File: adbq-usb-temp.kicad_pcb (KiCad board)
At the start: 4 copper layers, 75 parts, among them J4 USB_C_Receptacle_USB2.0_14P, Q1 Q_NMOS, Q2 Q_NMOS, Q3 Q_NMOS, SW1 SW_Push, SW2 TestPoint, SW3 TestPoint, SW4 TestPoint, U1 ESP32-S3FH4R2, U14 TMP117AIDRV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

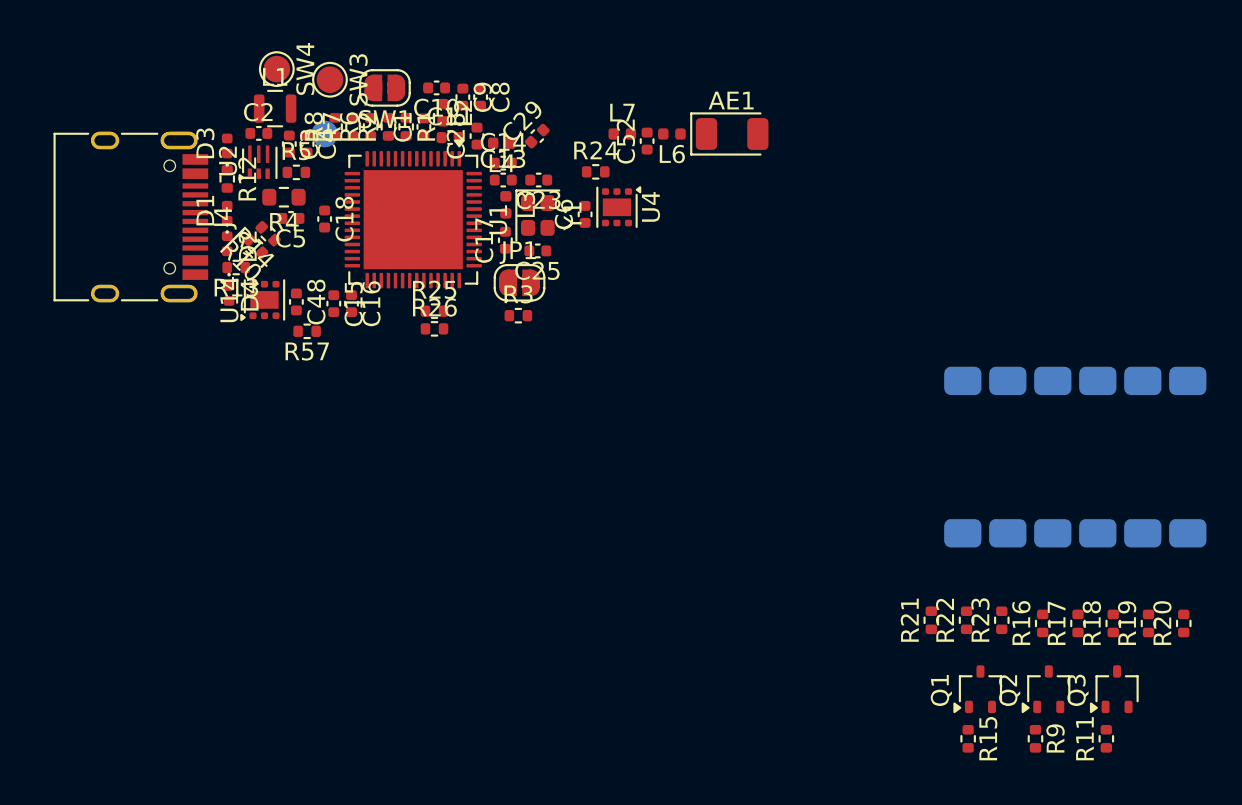
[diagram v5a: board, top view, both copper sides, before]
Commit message: pcb: add board outline
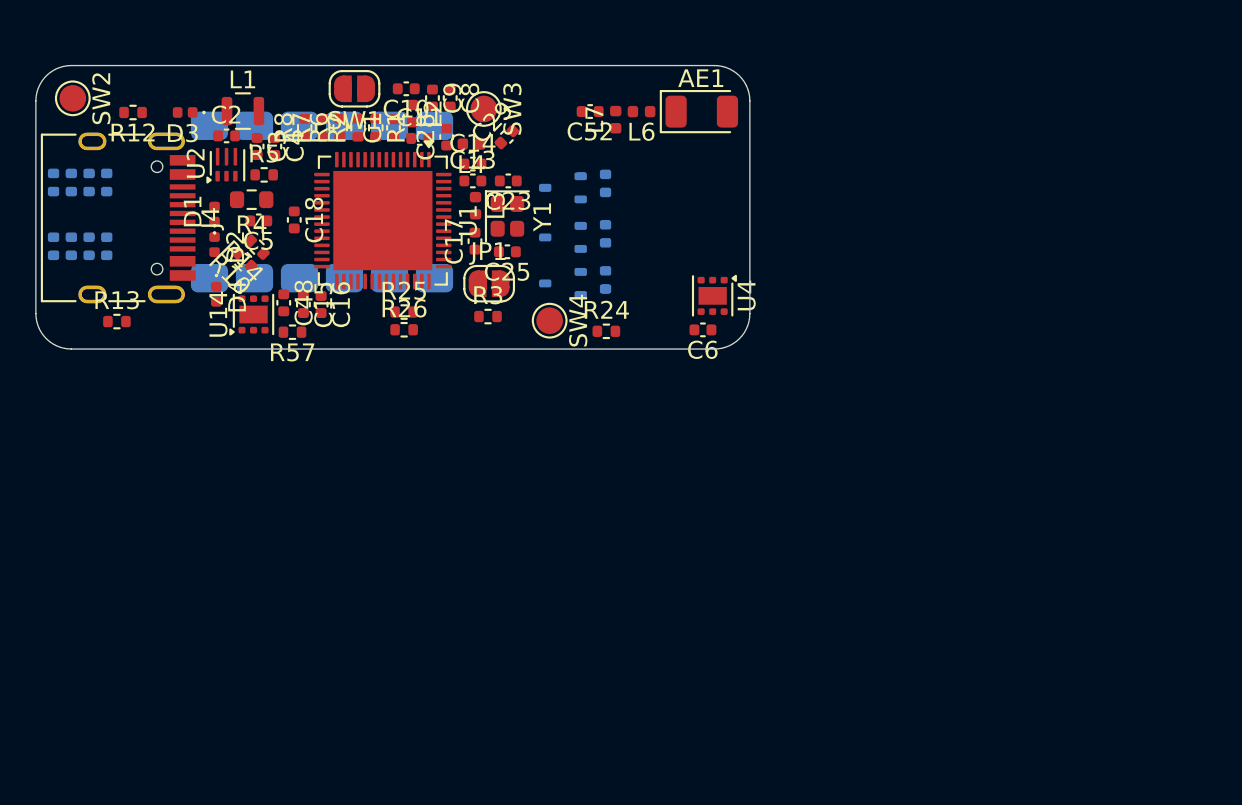
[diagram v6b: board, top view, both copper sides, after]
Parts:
- Q1, Q2, Q3, R11, R15, R16, R17, R18, R19, R20, R21, R22, R23, R9: moved to B.Cu
- SW2: moved to F.Cu
- moved R20 68.5 mm to (83.0, 93.6)
- moved R19 65.4 mm to (83.0, 97.2), turned to -90 degrees
- moved R18 61.6 mm to (85.0, 97.2), turned to -90 degrees
- moved R16 60.2 mm to (84.0, 93.6)
- moved R17 60.2 mm to (86.0, 93.6)
- moved R23 56.6 mm to (84.0, 97.2), turned to -90 degrees
- moved R21 53.6 mm to (85.0, 93.6)
- moved R22 52.9 mm to (86.0, 97.2), turned to -90 degrees
- moved U3 44.9 mm to (98.2, 94.7)
- moved Q3 38.8 mm to (111.8, 99.3), turned to 180 degrees
- moved R11 38.3 mm to (114.2, 99.1), turned to -90 degrees
- moved Q2 37.4 mm to (111.8, 96.7), turned to 180 degrees
- moved R15 37.4 mm to (114.2, 93.7)
- moved R9 37.4 mm to (114.2, 96.5)
- moved Q1 36.8 mm to (111.8, 93.9), turned to 180 degrees
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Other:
- board outline added: 40.3 x 16 mm

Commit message: pcb: add inner gnd planes
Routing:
- added copper zone on In1.Cu, net GND
- added copper zone on In2.Cu, net GND
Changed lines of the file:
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@@
+		)
+	)
+	(zone
+		(net 3)
+		(net_name "GND")
+		(layers "In1.Cu" "In2.Cu")
+		(hatch edge 0.5)
+		(connect_pads
+			(clearance 0.2)
+		)
+		(min_thickness 0.15)
+		(filled_areas_thickness no)
+		(fill yes
+			(thermal_gap 0.4)
+			(thermal_bridge_width 0.25)
+		)
+		(polygon
+			(pts
+				(xy 82 87) (xy 122.4 87) (xy 122.4 103) (xy 82 103)
+			)
 		)
 	)

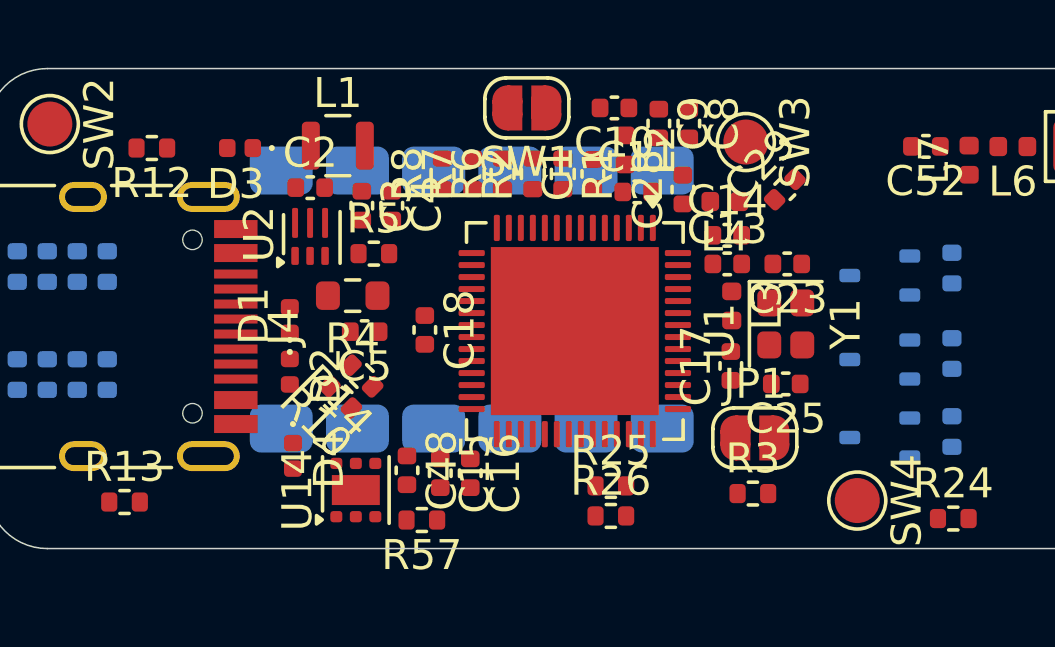
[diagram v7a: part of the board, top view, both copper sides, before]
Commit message: pcb: add tooling holes
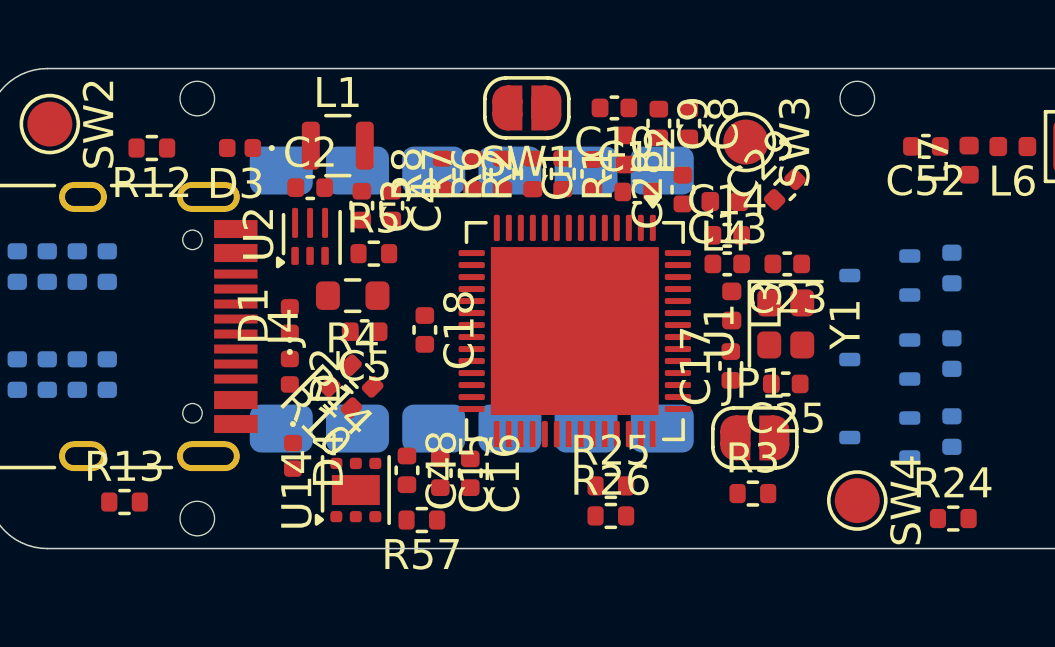
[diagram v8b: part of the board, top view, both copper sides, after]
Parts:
- added REF**: ToolingHole_1.152mm, MountingHole:ToolingHole_1.152mm, F.Cu at (111.0, 88.0)
- added REF**: ToolingHole_1.152mm, MountingHole:ToolingHole_1.152mm, F.Cu at (89.0, 102.0)
- added REF**: ToolingHole_1.152mm, MountingHole:ToolingHole_1.152mm, F.Cu at (89.0, 88.0)
